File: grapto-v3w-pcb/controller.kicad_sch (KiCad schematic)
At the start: 30 parts, among them J5 Conn_01x06_Female, J6 USB_C_Receptacle_USB2.0, J7 USB_C_Receptacle_USB2.0, J8 Conn_01x06_Male, U11 USBLC6-4SC6, U13 TPS2110, U14 LM3676SD-3.3

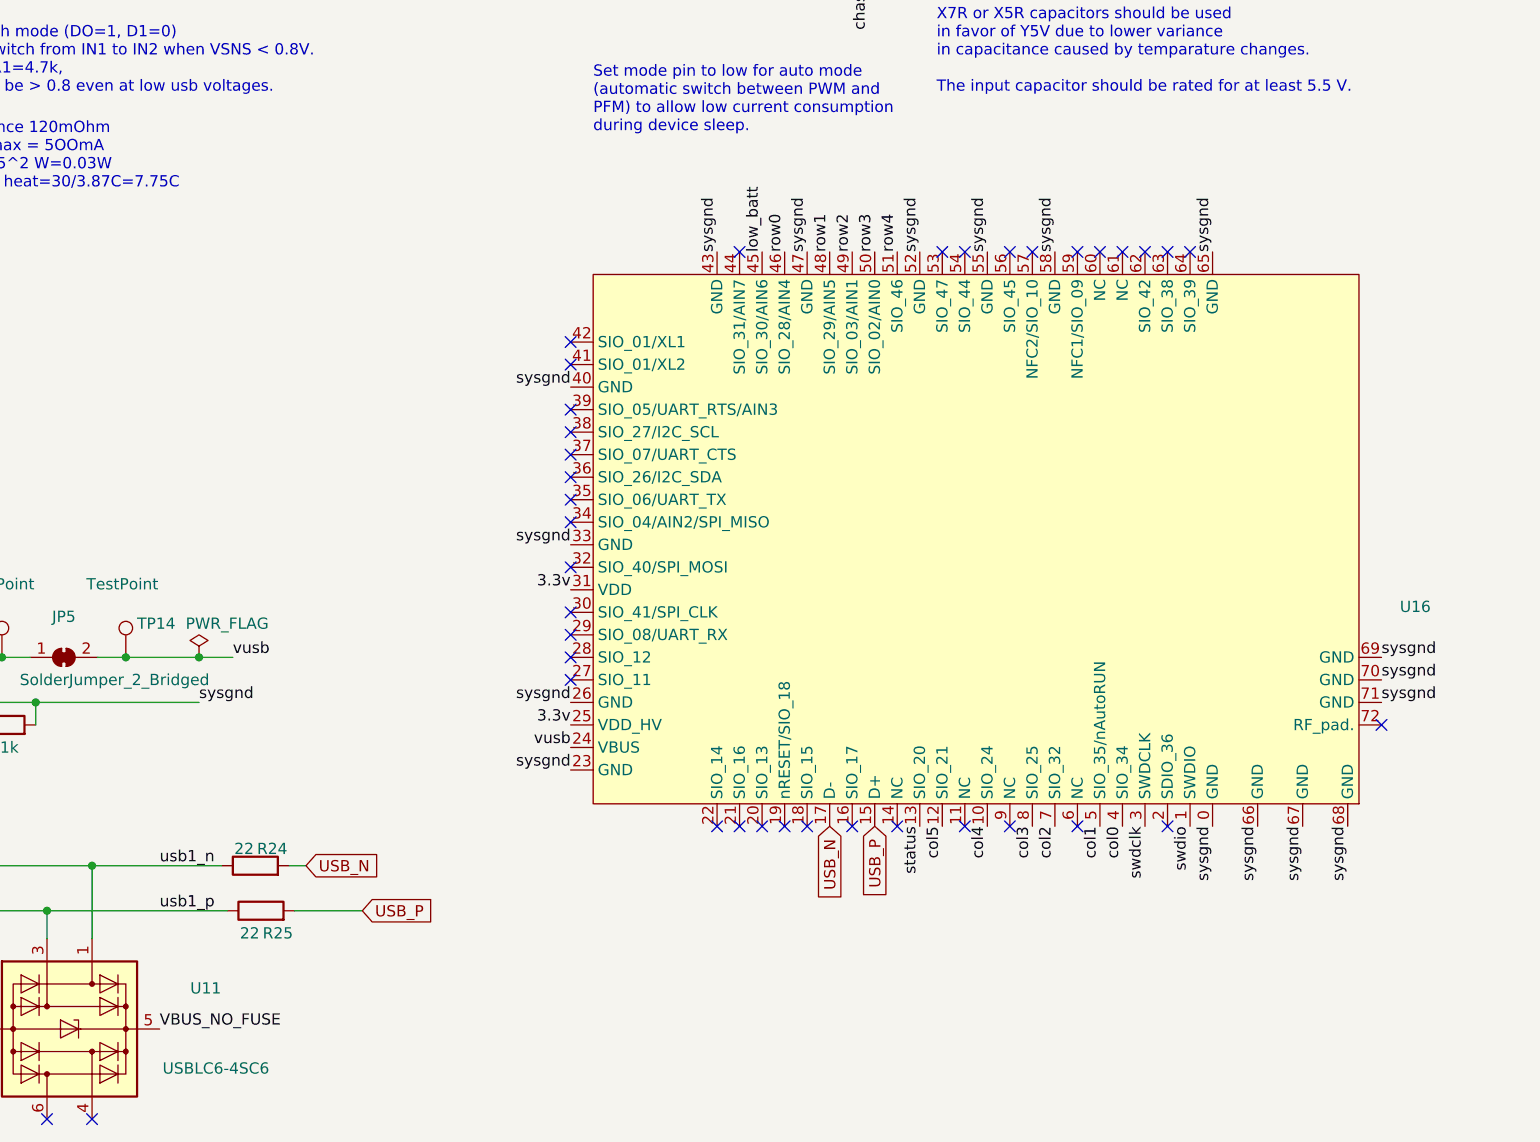
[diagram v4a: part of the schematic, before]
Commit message: Adjusting schematic to improve layout.
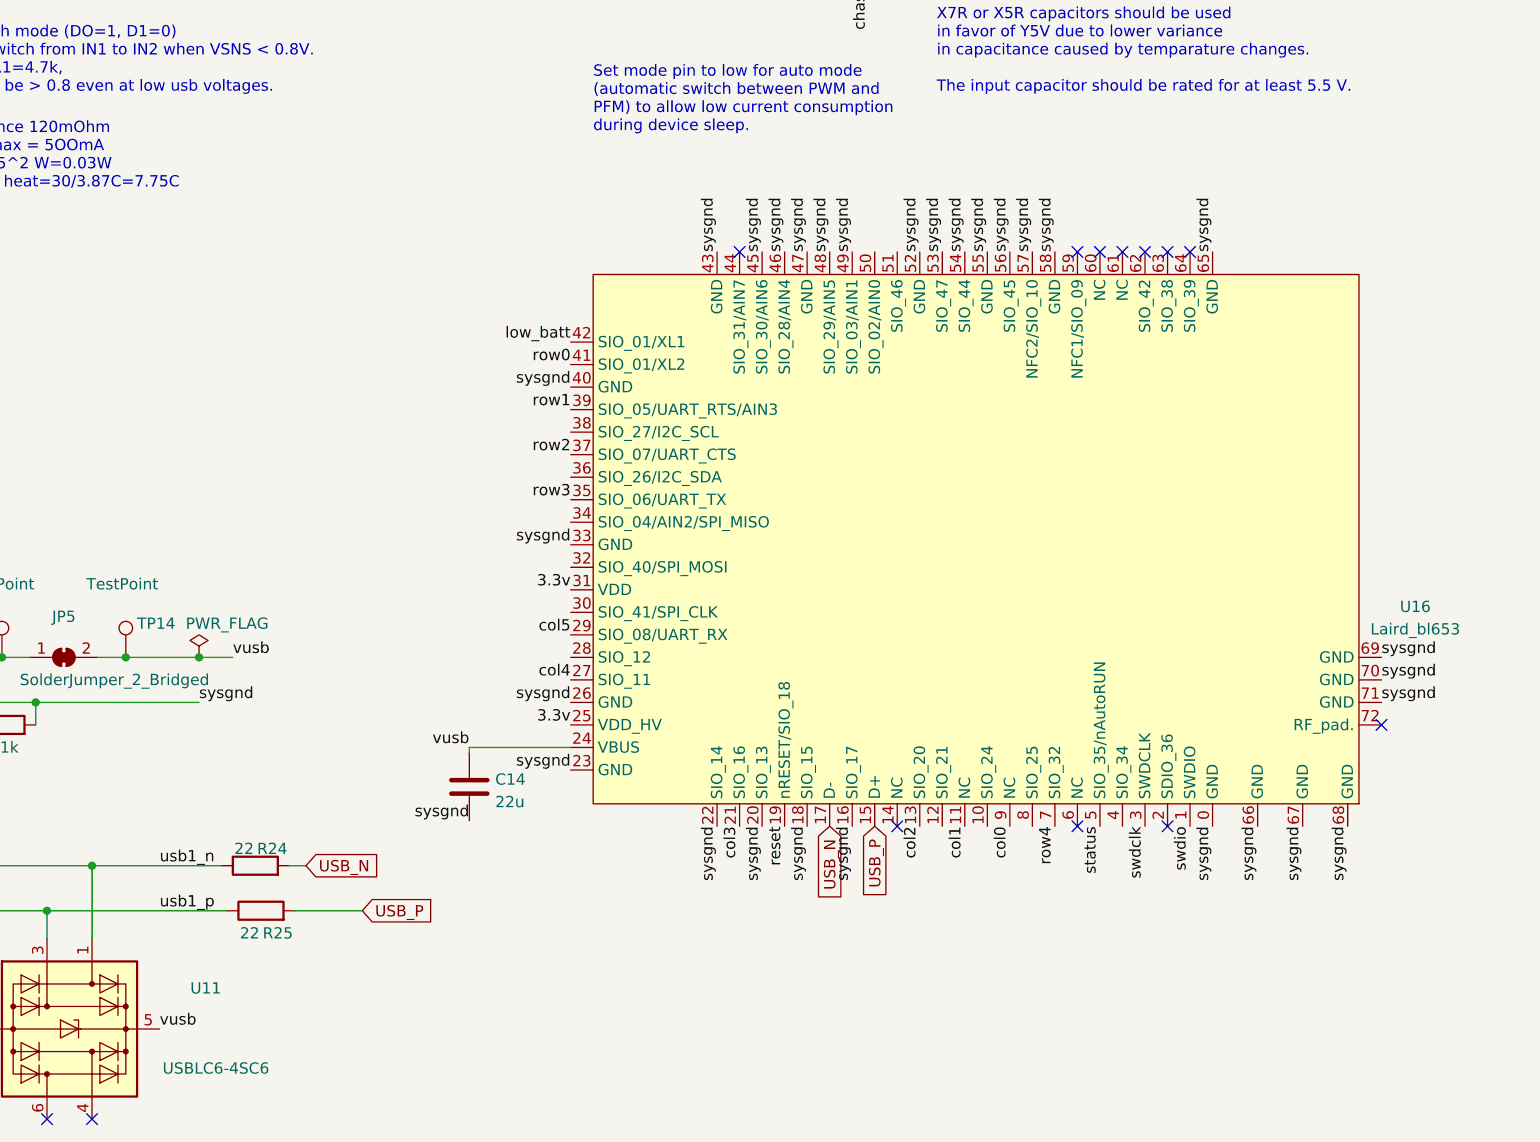
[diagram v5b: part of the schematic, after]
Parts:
- added C14: 22u, Fuse:Fuse_0603_1608Metric_Pad1.05x0.95mm_HandSolder, symbol Device:C
- U16: value (none) -> Laird_bl653; footprint (none) -> grapto-v3w:Laird_bl653
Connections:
- net VBUS_NO_FUSE: no longer U11.5 (VBUS)
- net col0: now also U16.9 (NC); no longer U16.4 (SIO_34)
- net col1: now also U16.11 (NC); no longer U16.5 (SIO_35/nAutoRUN)
- net col2: now also U16.13 (SIO_20); no longer U16.7 (SIO_32)
- net col3: now also U16.21 (SIO_16); no longer U16.8 (SIO_25)
- net col4: now also U16.27 (SIO_11); no longer U16.10 (SIO_24)
- net col5: now also U16.29 (SIO_08/UART_RX); no longer U16.12 (SIO_21)
- net low_batt: now also U16.42 (SIO_01/XL1); no longer U16.45 (SIO_30/AIN6)
- net reset: now also U16.19 (nRESET/SIO_18)
- net row0: now also U16.41 (SIO_01/XL2); no longer U16.46 (SIO_28/AIN4)
- net row1: now also U16.39 (SIO_05/UART_RTS/AIN3); no longer U16.48 (SIO_29/AIN5)
- net row2: now also U16.37 (SIO_07/UART_CTS); no longer U16.49 (SIO_03/AIN1)
- net row3: now also U16.35 (SIO_06/UART_TX); no longer U16.50 (SIO_02/AIN0)
- net row4: now also U16.7 (SIO_32); no longer U16.51 (SIO_46)
- net status: now also U16.5 (SIO_35/nAutoRUN); no longer U16.13 (SIO_20)
- net sysgnd: now also U16.16 (SIO_17), U16.18 (SIO_15), U16.20 (SIO_13), U16.22 (SIO_14), U16.45 (SIO_30/AIN6), U16.46 (SIO_28/AIN4), U16.48 (SIO_29/AIN5), U16.49 (SIO_03/AIN1), U16.53 (SIO_47), U16.54 (SIO_44), U16.56 (SIO_45), U16.57 (NFC2/SIO_10), C14.2
- net vusb: now also U11.5 (VBUS), C14.1
- no-connect marks 56 -> 31

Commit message: Left half 2 layer initial layout.
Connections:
- net 3.3v: no longer J8.6 (Pin_6)
- net col0: now also U16.37 (SIO_07/UART_CTS); no longer U16.9 (NC)
- net col1: now also U16.35 (SIO_06/UART_TX); no longer U16.11 (NC)
- net col2: now also U16.29 (SIO_08/UART_RX); no longer U16.13 (SIO_20)
- net col3: now also U16.27 (SIO_11); no longer U16.21 (SIO_16)
- net col4: now also U16.21 (SIO_16); no longer U16.27 (SIO_11)
- net col5: now also U16.13 (SIO_20); no longer U16.29 (SIO_08/UART_RX)
- net low_batt: now also U16.45 (SIO_30/AIN6); no longer U16.42 (SIO_01/XL1)
- net p+: now also J5.5 (Pin_5)
- net row0: now also U16.43 (GND); no longer U16.41 (SIO_01/XL2)
- net row1: now also U16.42 (SIO_01/XL1); no longer U16.39 (SIO_05/UART_RTS/AIN3)
- net row2: now also U16.41 (SIO_01/XL2); no longer U16.37 (SIO_07/UART_CTS)
- net row3: now also U16.39 (SIO_05/UART_RTS/AIN3); no longer U16.35 (SIO_06/UART_TX)
- net sysgnd: now also U16.12 (SIO_21), U16.2 (SDIO_36), U16.28 (SIO_12), U16.30 (SIO_41/SPI_CLK), U16.32 (SIO_40/SPI_MOSI), U16.38 (SIO_27/I2C_SCL), U16.44 (SIO_31/AIN7), U16.50 (SIO_02/AIN0), U16.51 (SIO_46), U16.62 (SIO_42), U16.63 (SIO_38), U16.64 (SIO_39), U16.8 (SIO_25); no longer U16.43 (GND), U16.45 (SIO_30/AIN6)
- no-connect marks 31 -> 25
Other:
- note added: "Use 3v3 from test point"
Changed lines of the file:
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@@
   (no_connect (at 50.8 142.24))
   (no_connect (at 50.8 137.16))
+  (no_connect (at 76.835 79.375))
   (no_connect (at 33.655 41.275))
-  (no_connect (at 33.655 36.195))
   (no_connect (at 126.365 189.23))
   (no_connect (at 121.285 189.23))
@@
   (no_connect (at 98.425 165.1))
   (no_connect (at 237.49 156.21))
-  (no_connect (at 247.65 156.21))
-  (no_connect (at 199.39 91.44))
   (no_connect (at 237.49 91.44))
-  (no_connect (at 247.65 91.44))
-  (no_connect (at 250.19 91.44))
-  (no_connect (at 245.11 91.44))
   (no_connect (at 242.57 91.44))
   (no_connect (at 240.03 91.44))
-  (no_connect (at 217.17 156.21))
   (no_connect (at 33.655 38.735))
   (no_connect (at 50.8 165.1))
@@
     (effects (font (size 1.27 1.27)) (justify left bottom))
   )
+  (text "Use 3v3 from test point" (at 66.675 76.2 0)
+    (effects (font (size 1.27 1.27)) (justify left bottom))
+  )
   (text "2.2 uH induction is chosen per datasheet recommendation.\nAlso, the saturation curren rating should be above\n1200mA which is the converters max current limit.\nThe inductor resistance should also be low."
     (at 196.85 37.465 0)
@@
     (effects (font (size 1.27 1.27)) (justify left bottom))
   )
-  (label "3.3v" (at 76.835 79.375 180)
+  (label "sysgnd" (at 180.34 132.08 180)
     (effects (font (size 1.27 1.27)) (justify right bottom))
   )
@@
     (effects (font (size 1.27 1.27)) (justify right bottom))
   )
+  (label "sysgnd" (at 250.19 91.44 90)
+    (effects (font (size 1.27 1.27)) (justify left bottom))
+  )
   (label "VBUS_NO_FUSE" (at 100.965 137.16 90)
     (effects (font (size 1.27 1.27)) (justify left bottom))
@@
     (effects (font (size 1.27 1.27)) (justify right bottom))
   )
+  (label "sysgnd" (at 232.41 156.21 270)
+    (effects (font (size 1.27 1.27)) (justify right bottom))
+  )
   (label "swdclk" (at 76.835 84.455 180)
     (effects (font (size 1.27 1.27)) (justify right bottom))
@@
     (effects (font (size 1.27 1.27)) (justify right bottom))
   )
+  (label "sysgnd" (at 214.63 91.44 90)
+    (effects (font (size 1.27 1.27)) (justify left bottom))
+  )
   (label "usb1_n" (at 133.985 160.655 0)
     (effects (font (size 1.27 1.27)) (justify left bottom))
@@
     (effects (font (size 1.27 1.27)) (justify right bottom))
   )
-  (label "col3" (at 199.39 156.21 270)
+  (label "col3" (at 180.34 139.7 180)
     (effects (font (size 1.27 1.27)) (justify right bottom))
   )
@@
     (effects (font (size 1.27 1.27)) (justify left bottom))
   )
+  (label "sysgnd" (at 199.39 91.44 90)
+    (effects (font (size 1.27 1.27)) (justify left bottom))
+  )
+  (label "sysgnd" (at 180.34 137.16 180)
+    (effects (font (size 1.27 1.27)) (justify right bottom))
+  )
   (label "col4" (at 27.94 90.805 180)
     (effects (font (size 1.27 1.27)) (justify right bottom))
   )
+  (label "sysgnd" (at 222.25 156.21 270)
+    (effects (font (size 1.27 1.27)) (justify right bottom))
+  )
   (label "status" (at 76.835 86.995 180)
     (effects (font (size 1.27 1.27)) (justify right bottom))
@@
     (effects (font (size 1.27 1.27)) (justify left bottom))
   )
-  (label "low_batt" (at 180.34 101.6 180)
-    (effects (font (size 1.27 1.27)) (justify right bottom))
+  (label "low_batt" (at 201.93 91.44 90)
+    (effects (font (size 1.27 1.27)) (justify left bottom))
   )
   (label "chassi" (at 213.995 60.96 270)
@@
     (effects (font (size 1.27 1.27)) (justify right bottom))
   )
+  (label "sysgnd" (at 247.65 91.44 90)
+    (effects (font (size 1.27 1.27)) (justify left bottom))
+  )
   (label "sysgnd" (at 189.865 54.61 180)
     (effects (font (size 1.27 1.27)) (justify right bottom))
   )
-  (label "col2" (at 219.71 156.21 270)
+  (label "sysgnd" (at 217.17 91.44 90)
+    (effects (font (size 1.27 1.27)) (justify left bottom))
+  )
+  (label "sysgnd" (at 180.34 127 180)
+    (effects (font (size 1.27 1.27)) (justify right bottom))
+  )
+  (label "col2" (at 180.34 134.62 180)
     (effects (font (size 1.27 1.27)) (justify right bottom))
   )
@@
     (effects (font (size 1.27 1.27)) (justify left bottom))
   )
-  (label "row0" (at 180.34 104.14 180)
-    (effects (font (size 1.27 1.27)) (justify right bottom))
+  (label "row0" (at 196.85 91.44 90)
+    (effects (font (size 1.27 1.27)) (justify left bottom))
   )
   (label "row4" (at 234.95 156.21 270)
     (effects (font (size 1.27 1.27)) (justify right bottom))
   )
-  (label "row1" (at 180.34 109.22 180)
+  (label "row1" (at 180.34 101.6 180)
     (effects (font (size 1.27 1.27)) (justify right bottom))
   )
@@
     (effects (font (size 1.27 1.27)) (justify right bottom))
   )
-  (label "col4" (at 180.34 139.7 180)
-    (effects (font (size 1.27 1.27)) (justify right bottom))
-  )
-  (label "col0" (at 229.87 156.21 270)
+  (label "col4" (at 199.39 156.21 270)
+    (effects (font (size 1.27 1.27)) (justify right bottom))
+  )
+  (label "col0" (at 180.34 114.3 180)
     (effects (font (size 1.27 1.27)) (justify right bottom))
   )
@@
     (effects (font (size 1.27 1.27)) (justify left bottom))
   )
-  (label "row3" (at 180.34 119.38 180)
+  (label "row3" (at 180.34 109.22 180)
     (effects (font (size 1.27 1.27)) (justify right bottom))
   )
@@
     (effects (font (size 1.27 1.27)) (justify left bottom))
   )
+  (label "sysgnd" (at 180.34 111.76 180)
+    (effects (font (size 1.27 1.27)) (justify right bottom))
+  )
   (label "col3" (at 27.94 88.265 180)
     (effects (font (size 1.27 1.27)) (justify right bottom))
@@
     (effects (font (size 1.27 1.27)) (justify right bottom))
   )
+  (label "sysgnd" (at 247.65 156.21 270)
+    (effects (font (size 1.27 1.27)) (justify right bottom))
+  )
   (label "sysgnd" (at 252.73 91.44 90)
     (effects (font (size 1.27 1.27)) (justify left bottom))
@@
     (effects (font (size 1.27 1.27)) (justify right bottom))
   )
-  (label "row2" (at 180.34 114.3 180)
+  (label "row2" (at 180.34 104.14 180)
     (effects (font (size 1.27 1.27)) (justify right bottom))
   )
@@
     (effects (font (size 1.27 1.27)) (justify right bottom))
   )
-  (label "sysgnd" (at 196.85 91.44 90)
+  (label "sysgnd" (at 245.11 91.44 90)
     (effects (font (size 1.27 1.27)) (justify left bottom))
   )
@@
     (effects (font (size 1.27 1.27)) (justify left bottom))
   )
-  (label "col1" (at 224.79 156.21 270)
+  (label "col1" (at 180.34 119.38 180)
     (effects (font (size 1.27 1.27)) (justify right bottom))
   )
@@
     (effects (font (size 1.27 1.27)) (justify right bottom))
   )
+  (label "p+" (at 33.655 36.195 0)
+    (effects (font (size 1.27 1.27)) (justify left bottom))
+  )
   (label "row3" (at 46.355 88.265 0)
     (effects (font (size 1.27 1.27)) (justify left bottom))
@@
     (effects (font (size 1.27 1.27)) (justify right bottom))
   )
-  (label "sysgnd" (at 201.93 91.44 90)
-    (effects (font (size 1.27 1.27)) (justify left bottom))
-  )
-  (label "col5" (at 180.34 134.62 180)
-    (effects (font (size 1.27 1.27)) (justify right bottom))
-  )
+  (label "col5" (at 219.71 156.21 270)
+    (effects (font (size 1.27 1.27)) (justify right bottom))
+  )

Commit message: Initial 2 layer layout right.
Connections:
- net 3.3v: now also U16.32 (SIO_40/SPI_MOSI)
- net col1: now also U16.36 (SIO_26/I2C_SDA)
- net row0: now also U16.46 (SIO_28/AIN4); no longer U16.43 (GND)
- net sysgnd: now also U16.34 (SIO_04/AIN2/SPI_MISO), U16.43 (GND), U16.59 (NFC1/SIO_09); no longer U16.32 (SIO_40/SPI_MOSI), U16.46 (SIO_28/AIN4)
- no-connect marks 25 -> 29
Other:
- note added: "TODO disable pullups on grounded GPIOs"

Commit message: 2-layer layout ready to order.
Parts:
- TP13, TP14, TP15, TP16, TP17, TP18, TP22: footprint TestPoint:TestPoint_THTPad_D2.0mm_Drill1.0mm -> grapto-v3w:TestPoint_THTPad_D2.0mm_Drill1.0mm
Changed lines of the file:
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@@
       (effects (font (size 1.27 1.27)) (justify left))
     )
-    (property "Footprint" "TestPoint:TestPoint_THTPad_D2.0mm_Drill1.0mm" (id 2) (at 255.905 46.99 0)
+    (property "Footprint" "grapto-v3w:TestPoint_THTPad_D2.0mm_Drill1.0mm" (id 2) (at 255.905 46.99 0)
       (effects (font (size 1.27 1.27)) hide)
     )
@@
     (property "Reference" "TP22" (id 0) (at 80.01 27.305 90))
     (property "Value" "~" (id 1) (at 77.47 30.48 90))
-    (property "Footprint" "TestPoint:TestPoint_THTPad_D2.0mm_Drill1.0mm" (id 2) (at 84.455 33.655 0)
+    (property "Footprint" "grapto-v3w:TestPoint_THTPad_D2.0mm_Drill1.0mm" (id 2) (at 84.455 33.655 0)
       (effects (font (size 1.27 1.27)) hide)
     )
@@
       (effects (font (size 1.27 1.27)) (justify left))
     )
-    (property "Footprint" "TestPoint:TestPoint_THTPad_D2.0mm_Drill1.0mm" (id 2) (at 94.615 177.165 0)
+    (property "Footprint" "grapto-v3w:TestPoint_THTPad_D2.0mm_Drill1.0mm" (id 2) (at 94.615 177.165 0)
       (effects (font (size 1.27 1.27)) hide)
     )
@@
       (effects (font (size 1.27 1.27)) (justify left))
     )
-    (property "Footprint" "TestPoint:TestPoint_THTPad_D2.0mm_Drill1.0mm" (id 2) (at 135.255 137.16 0)
+    (property "Footprint" "grapto-v3w:TestPoint_THTPad_D2.0mm_Drill1.0mm" (id 2) (at 135.255 137.16 0)
       (effects (font (size 1.27 1.27)) hide)
     )
@@
       (effects (font (size 1.27 1.27)) (justify left))
     )
-    (property "Footprint" "TestPoint:TestPoint_THTPad_D2.0mm_Drill1.0mm" (id 2) (at 121.285 137.16 0)
+    (property "Footprint" "grapto-v3w:TestPoint_THTPad_D2.0mm_Drill1.0mm" (id 2) (at 121.285 137.16 0)
       (effects (font (size 1.27 1.27)) hide)
     )
@@
       (effects (font (size 1.27 1.27)) (justify left))
     )
-    (property "Footprint" "TestPoint:TestPoint_THTPad_D2.0mm_Drill1.0mm" (id 2) (at 200.025 46.99 0)
+    (property "Footprint" "grapto-v3w:TestPoint_THTPad_D2.0mm_Drill1.0mm" (id 2) (at 200.025 46.99 0)
       (effects (font (size 1.27 1.27)) hide)
     )
@@
       (effects (font (size 1.27 1.27)) (justify left))
     )
-    (property "Footprint" "TestPoint:TestPoint_THTPad_D2.0mm_Drill1.0mm" (id 2) (at 269.875 46.99 0)
-      (effects (font (size 1.27 1.27)) hide)
-    )
+    (property "Footprint" "grapto-v3w:TestPoint_THTPad_D2.0mm_Drill1.0mm" (id 2) (at 269.875 46.99 0)
+      (effects (font (size 1.27 1.27)) hide)
+    )
